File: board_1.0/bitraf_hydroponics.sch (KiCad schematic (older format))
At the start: 40 parts, among them P1 12V, P10 I2C_4, P11 BUZZ, P12 LDR, P13 TEMP_HUM, P14 PROGRAMMER, P15 LCD, P16 RADIO_433, P2 SWITCH_1, P3 SWITCH_2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

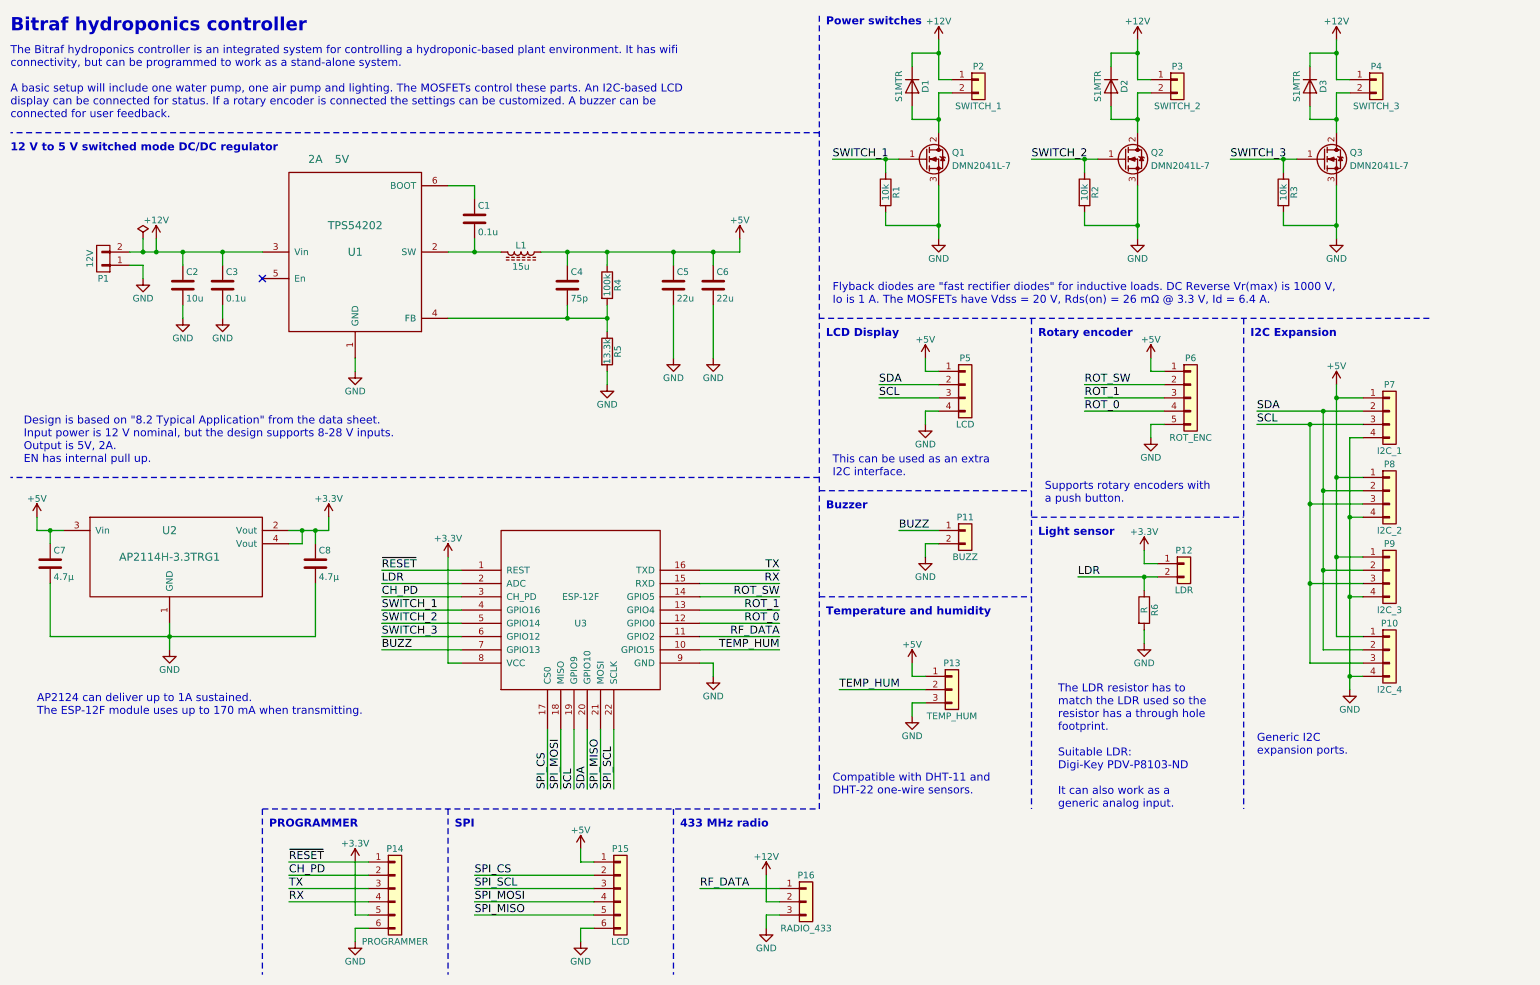
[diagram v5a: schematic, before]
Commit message: everything connected. Ugly and thin tracks where they should be wider, but passes test.
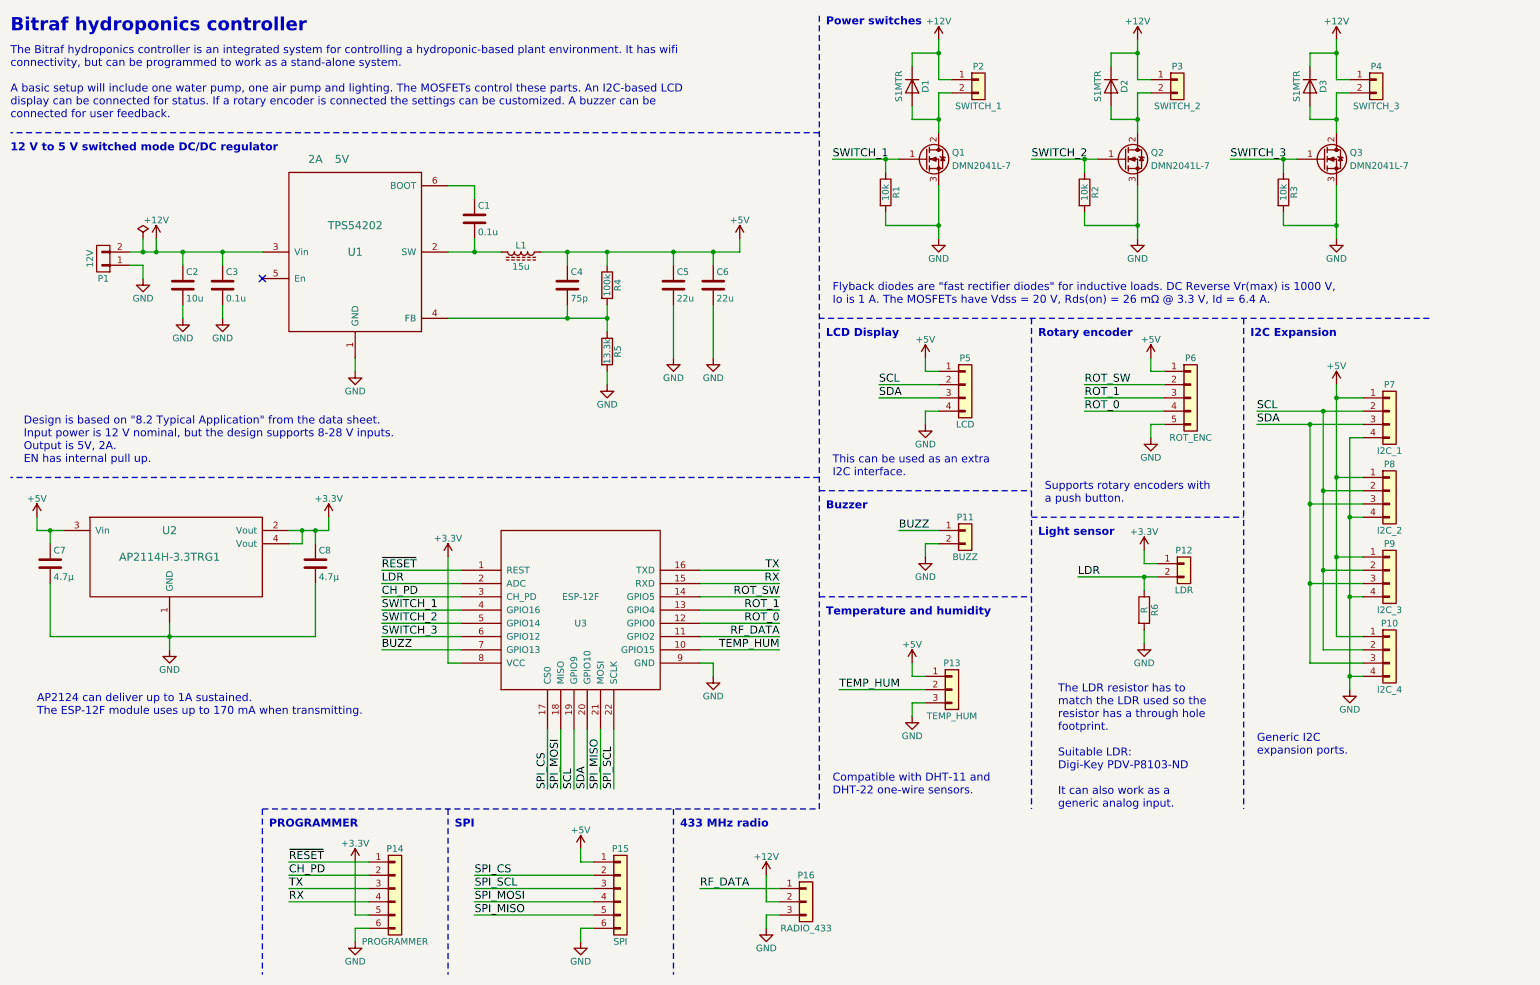
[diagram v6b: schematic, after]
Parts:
- P15: value LCD -> SPI
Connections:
- net SCL: now also P10.2 (Pin_2), P5.2 (Pin_2), P7.2 (Pin_2), P8.2 (Pin_2), P9.2 (Pin_2); no longer P10.3 (Pin_3), P5.3 (Pin_3), P7.3 (Pin_3), P8.3 (Pin_3), P9.3 (Pin_3)
- net SDA: now also P10.3 (Pin_3), P5.3 (Pin_3), P7.3 (Pin_3), P8.3 (Pin_3), P9.3 (Pin_3); no longer P10.2 (Pin_2), P5.2 (Pin_2), P7.2 (Pin_2), P8.2 (Pin_2), P9.2 (Pin_2)
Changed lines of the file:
@@
 	1    0    0    -1
 $EndComp
+Text Label 7050 3300 0    60   ~ 0
+SCL
 Text Label 7050 3400 0    60   ~ 0
-SCL
-Text Label 7050 3300 0    60   ~ 0
 SDA
 $Comp
@@
 	1    0    0    -1
 $EndComp
-Text Label 9900 3500 0    60   ~ 0
+Text Label 9900 3600 0    60   ~ 0
 SDA
 Text Label 3300 4800 0    60   ~ 0
@@
 	1    0    0    -1
 $EndComp
-Text Label 9900 3600 0    60   ~ 0
+Text Label 9900 3500 0    60   ~ 0
 SCL
 Text Notes 9900 6100 0    60   ~ 0
@@
 	7600 1100 7500 1100
 Wire Wire Line
-	7500 1100 7500 1300
-Wire Wire Line
-	7500 1300 7500 1400
+	7500 1100 7500 1400
 Wire Wire Line
 	7500 1000 7600 1000
 Wire Wire Line
-	7500 700  7500 800
-Wire Wire Line
-	7500 800  7500 1000
+	7500 700  7500 1000
 Wire Wire Line
 	7300 1200 7300 1300
@@
 Connection ~ 7500 800
 Wire Wire Line
-	7500 1800 7500 2100
-Wire Wire Line
-	7500 2100 7500 2200
-Wire Wire Line
-	6700 1600 7100 1600
-Wire Wire Line
-	7100 1600 7200 1600
+	7500 1800 7500 2200
+Wire Wire Line
+	6700 1600 7200 1600
 Wire Wire Line
 	7100 1700 7100 1600
@@
 	9100 1100 9000 1100
 Wire Wire Line
-	9000 1100 9000 1300
-Wire Wire Line
-	9000 1300 9000 1400
+	9000 1100 9000 1400
 Wire Wire Line
 	9000 1000 9100 1000
 Wire Wire Line
-	9000 700  9000 800
-Wire Wire Line
-	9000 800  9000 1000
+	9000 700  9000 1000
 Wire Wire Line
 	8800 1200 8800 1300
@@
 Connection ~ 9000 800
 Wire Wire Line
-	9000 1800 9000 2100
-Wire Wire Line
-	9000 2100 9000 2200
-Wire Wire Line
-	8200 1600 8600 1600
-Wire Wire Line
-	8600 1600 8700 1600
+	9000 1800 9000 2200
+Wire Wire Line
+	8200 1600 8700 1600
 Wire Wire Line
 	8600 1700 8600 1600
@@
 	10600 1100 10500 1100
 Wire Wire Line
-	10500 1100 10500 1300
-Wire Wire Line
-	10500 1300 10500 1400
+	10500 1100 10500 1400
 Wire Wire Line
 	10500 1000 10600 1000
 Wire Wire Line
-	10500 700  10500 800
-Wire Wire Line
-	10500 800  10500 1000
+	10500 700  10500 1000
 Wire Wire Line
 	10300 1200 10300 1300
@@
 	10300 900  10300 800
 Wire Wire Line
-	10500 1800 10500 2100
-Wire Wire Line
-	10500 2100 10500 2200
-Wire Wire Line
-	9700 1600 10100 1600
-Wire Wire Line
-	10100 1600 10200 1600
+	10500 1800 10500 2200
+Wire Wire Line
+	9700 1600 10200 1600
 Wire Wire Line
 	10100 1700 10100 1600
@@
 	9200 3500 8600 3500
 Wire Wire Line
-	1400 2300 1500 2300
-Wire Wire Line
-	1500 2300 1600 2300
-Wire Wire Line
-	1600 2300 1800 2300
-Wire Wire Line
-	1800 2300 2100 2300
-Wire Wire Line
-	2100 2300 2400 2300
+	1400 2300 2400 2300
 Wire Wire Line
 	1600 2300 1600 2200
@@
 	7500 4400 7200 4400
 Wire Wire Line
-	8550 4750 9050 4750
-Wire Wire Line
-	9050 4750 9150 4750
+	8550 4750 9150 4750
 Wire Wire Line
 	9050 4750 9050 4850
@@
 	10400 5300 10700 5300
 Wire Wire Line
-	10500 3300 10500 3400
-Wire Wire Line
-	10500 3400 10500 4000
-Wire Wire Line
-	10500 4000 10500 4600
-Wire Wire Line
-	10500 4600 10500 5200
+	10500 3300 10500 5200
 Wire Wire Line
 	10600 5500 10700 5500
@@
 	10400 4100 10700 4100
 Wire Wire Line
-	9900 3600 10300 3600
-Wire Wire Line
-	10300 3600 10700 3600
-Wire Wire Line
-	9900 3500 10400 3500
-Wire Wire Line
-	10400 3500 10700 3500
+	9900 3600 10700 3600
+Wire Wire Line
+	9900 3500 10700 3500
 Wire Wire Line
 	10500 3400 10700 3400
@@
 	8800 1300 9000 1300
 Wire Wire Line
-	3800 2300 4000 2300
-Wire Wire Line
-	4000 2300 4200 2300
-Wire Wire Line
-	4500 2300 4700 2300
-Wire Wire Line
-	4700 2300 5000 2300
-Wire Wire Line
-	5000 2300 5500 2300
-Wire Wire Line
-	5500 2300 5800 2300
-Wire Wire Line
-	5800 2300 6000 2300
+	3800 2300 4200 2300
+Wire Wire Line
+	4500 2300 6000 2300
 Wire Wire Line
 	5000 3200 5000 3300
@@
 	5500 3100 5500 2700
 Wire Wire Line
-	10400 3500 10400 4100
-Wire Wire Line
-	10400 4100 10400 4700
-Wire Wire Line
-	10400 4700 10400 5300
+	10400 3500 10400 5300
 Connection ~ 10400 4100
 Connection ~ 10400 3500
 Connection ~ 10400 4700
 Wire Wire Line
-	10300 3600 10300 4200
-Wire Wire Line
-	10300 4200 10300 4800
-Wire Wire Line
-	10300 4800 10300 5400
+	10300 3600 10300 5400
 Connection ~ 10300 4800
 Connection ~ 10300 4200
@@
 	10600 3700 10700 3700
 Wire Wire Line
-	10600 3700 10600 4300
-Wire Wire Line
-	10600 4300 10600 4900
-Wire Wire Line
-	10600 4900 10600 5500
-Wire Wire Line
-	10600 5500 10600 5600
+	10600 3700 10600 5600
 Wire Notes Line
 	11200 2800 6600 2800
@@
 P 5100 7100
 F 0 "P15" H 5100 7400 50  0000 C CNN
-F 1 "LCD" H 5100 6700 50  0000 C CNN
+F 1 "SPI" H 5100 6700 50  0000 C CNN
 F 2 "Pin_Headers:Pin_Header_Straight_1x06_Pitch2.54mm" H 5100 7100 50  0001 C CNN
 F 3 "" H 5100 7100 50  0001 C CNN
@@
 $EndComp
 Wire Wire Line
-	5000 2700 5000 2800
-Wire Wire Line
-	5000 2800 5000 2900
-Wire Wire Line
-	3800 2800 4700 2800
-Wire Wire Line
-	4700 2800 5000 2800
+	5000 2700 5000 2900
+Wire Wire Line
+	3800 2800 5000 2800
 Wire Wire Line
 	4700 2800 4700 2700
@@
 	700  4300 700  4400
 Wire Wire Line
-	700  4400 800  4400
-Wire Wire Line
-	800  4400 900  4400
-Wire Wire Line
-	2600 4400 2700 4400
-Wire Wire Line
-	2700 4400 2800 4400
-Wire Wire Line
-	2800 4400 2900 4400
+	700  4400 900  4400
+Wire Wire Line
+	2600 4400 2900 4400
 Wire Wire Line
 	2900 4400 2900 4300
@@
 $EndComp
 Wire Wire Line
-	1700 5100 1700 5200
-Wire Wire Line
-	1700 5200 1700 5300
+	1700 5100 1700 5300
 $Comp
 L C C7
@@
 	800  4800 800  5200
 Wire Wire Line
-	800  5200 1700 5200
-Wire Wire Line
-	1700 5200 2800 5200
+	800  5200 2800 5200
 Connection ~ 1700 5200
 $Comp

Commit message: o Updating the symbol of P1 so it matches the other symbols.
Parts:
- P1: symbol CONN_01X02 -> Conn_01x02
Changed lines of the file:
@@
 LIBS:nodemcu
 LIBS:tps54202
+LIBS:ESP8266
 LIBS:ap2114
 LIBS:bitraf_hydroponics-cache
@@
 $EndComp
 $Comp
-L CONN_01X02 P1
+L Conn_01x02 P1
 U 1 1 57E46A8E
-P 1200 2350
+P 1200 2400
 F 0 "P1" H 1200 2500 50  0000 C CNN
-F 1 "12V" V 1300 2350 50  0000 C CNN
-F 2 "Connectors_Phoenix:PhoenixContact_PTSM0,5_4-HV-2,5_SMD" H 1200 2350 50  0001 C CNN
-F 3 "" H 1200 2350 50  0000 C CNN
-	1    1200 2350
+F 1 "12V" H 1200 2200 50  0000 C CNN
+F 2 "Connectors_Phoenix:PhoenixContact_PTSM0,5_4-HV-2,5_SMD" H 1200 2400 50  0001 C CNN
+F 3 "" H 1200 2400 50  0001 C CNN
+	1    1200 2400
 	-1   0    0    1
 $EndComp

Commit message: o Switching from PhoenixContact_PTSM0,5_4-HV-2,5_SMD to PhoenixContact_PTSM0,5_2-2,5-H_SMD.
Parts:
- P1, P11, P12, P2, P3, P4: footprint Connectors_Phoenix:PhoenixContact_PTSM0,5_4-HV-2,5_SMD -> Bitraf:PhoenixContact_PTSM0,5_2-2,5-H_SMD
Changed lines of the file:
@@
 LIBS:contrib
 LIBS:valves
-LIBS:nodemcu
 LIBS:tps54202
 LIBS:ESP8266
@@
 F 0 "P2" H 7800 1100 50  0000 C CNN
 F 1 "SWITCH_1" H 7800 800 50  0000 C CNN
-F 2 "Connectors_Phoenix:PhoenixContact_PTSM0,5_4-HV-2,5_SMD" H 7800 1000 50  0001 C CNN
+F 2 "Bitraf:PhoenixContact_PTSM0,5_2-2,5-H_SMD" H 7800 1000 50  0001 C CNN
 F 3 "" H 7800 1000 50  0001 C CNN
 	1    7800 1000
@@
 F 0 "P3" H 9300 1100 50  0000 C CNN
 F 1 "SWITCH_2" H 9300 800 50  0000 C CNN
-F 2 "Connectors_Phoenix:PhoenixContact_PTSM0,5_4-HV-2,5_SMD" H 9300 1000 50  0001 C CNN
+F 2 "Bitraf:PhoenixContact_PTSM0,5_2-2,5-H_SMD" H 9300 1000 50  0001 C CNN
 F 3 "" H 9300 1000 50  0001 C CNN
 	1    9300 1000
@@
 F 0 "P4" H 10800 1100 50  0000 C CNN
 F 1 "SWITCH_3" H 10800 800 50  0000 C CNN
-F 2 "Connectors_Phoenix:PhoenixContact_PTSM0,5_4-HV-2,5_SMD" H 10800 1000 50  0001 C CNN
+F 2 "Bitraf:PhoenixContact_PTSM0,5_2-2,5-H_SMD" H 10800 1000 50  0001 C CNN
 F 3 "" H 10800 1000 50  0001 C CNN
 	1    10800 1000
@@
 F 0 "P1" H 1200 2500 50  0000 C CNN
 F 1 "12V" H 1200 2200 50  0000 C CNN
-F 2 "Connectors_Phoenix:PhoenixContact_PTSM0,5_4-HV-2,5_SMD" H 1200 2400 50  0001 C CNN
+F 2 "Bitraf:PhoenixContact_PTSM0,5_2-2,5-H_SMD" H 1200 2400 50  0001 C CNN
 F 3 "" H 1200 2400 50  0001 C CNN
 	1    1200 2400
@@
 F 0 "P11" H 7700 4500 50  0000 C CNN
 F 1 "BUZZ" H 7700 4200 50  0000 C CNN
-F 2 "Connectors_Phoenix:PhoenixContact_PTSM0,5_4-HV-2,5_SMD" H 7700 4400 50  0001 C CNN
+F 2 "Bitraf:PhoenixContact_PTSM0,5_2-2,5-H_SMD" H 7700 4400 50  0001 C CNN
 F 3 "" H 7700 4400 50  0001 C CNN
 	1    7700 4400
@@
 F 0 "P12" H 9350 4750 50  0000 C CNN
 F 1 "LDR" H 9350 4450 50  0000 C CNN
-F 2 "Connectors_Phoenix:PhoenixContact_PTSM0,5_4-HV-2,5_SMD" H 9350 4650 50  0001 C CNN
+F 2 "Bitraf:PhoenixContact_PTSM0,5_2-2,5-H_SMD" H 9350 4650 50  0001 C CNN
 F 3 "" H 9350 4650 50  0001 C CNN
 	1    9350 4650
